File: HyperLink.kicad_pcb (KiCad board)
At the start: 2 copper layers, 35 x 24 mm, 41 parts, among them J1 USB_C_Receptacle_USB2.0, J2 Conn_02x05_Odd_Even, J3 Conn_02x05_Odd_Even, SW1 SW_Push, U1 ESP32-C3, U2 LM2937xMP, Y1 ABM11W-40.0000MHZ-8-B1U-T3

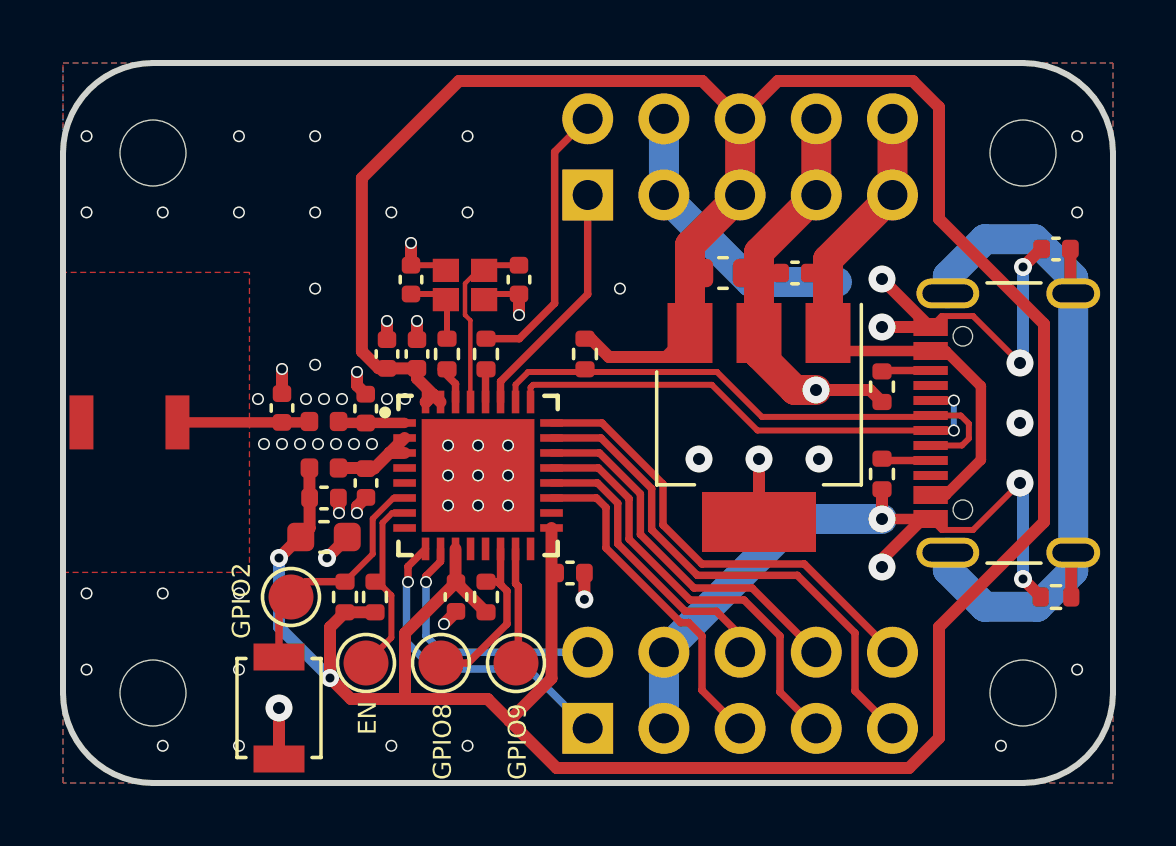
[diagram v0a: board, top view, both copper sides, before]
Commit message: Replace LDO and add USB TVS diode
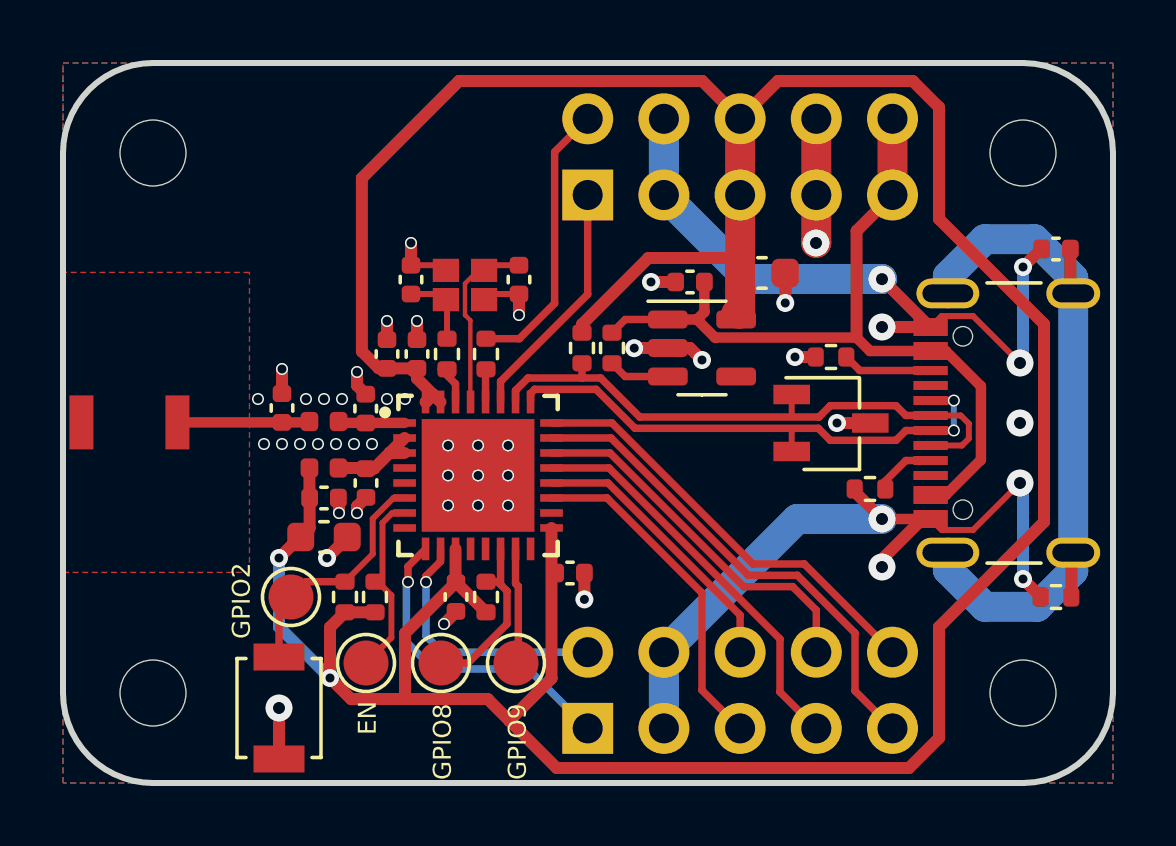
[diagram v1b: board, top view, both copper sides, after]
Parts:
- removed C13: 10u, Capacitor_SMD:C_0603_1608Metric
- added C7: 10u, Capacitor_SMD:C_0603_1608Metric, F.Cu at (142.3, 77.0)
- added R10: 10k, Resistor_SMD:R_0402_1005Metric, F.Cu at (137.3, 79.5)
- added U3: MIC5504-3.3YM5, Package_TO_SOT_SMD:SOT-23-5, F.Cu at (140.3, 79.5)
- C12: value 100n -> 1u
- U2: value LM2937xMP -> PESD2USB5UXT; footprint Package_TO_SOT_SMD:SOT-223-3_TabPin2 -> Package_TO_SOT_SMD:TSOT-23
- moved C12 3.51 mm to (139.9, 77.3)
- moved U2 2.40 mm to (144.6, 82.0), turned to 0 degrees
- moved R7 1.97 mm to (144.6, 79.8), turned to 180 degrees
- moved R8 0.64 mm to (145.9, 84.2), turned to 180 degrees
- moved R9 0.22 mm to (136.3, 79.5)
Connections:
- U2 pad 1: VBUS -> /USB_D+
- U2 pad 2: GND -> /USB_D-
- U2 pad 3: +3V3 -> GND
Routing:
- net VBUS: track 18.5 -> 27.2 mm
- net GND: track 74.6 -> 70.0 mm, vias 73 -> 50
- net /LDO_EN: track 0.00 -> 2.04 mm
- net /CC2: track 1.63 -> 3.00 mm
- net /USB_D+: track 18.5 -> 19.8 mm
- net +3V3: track 115.1 -> 116.2 mm
- net /GPIO14: track 14.3 -> 13.5 mm
- net /GPIO17: track 15.3 -> 14.5 mm
- net /GPIO16: track 17.3 -> 16.5 mm
- net /USB_D-: track 17.0 -> 17.8 mm

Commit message: Add status LEDs
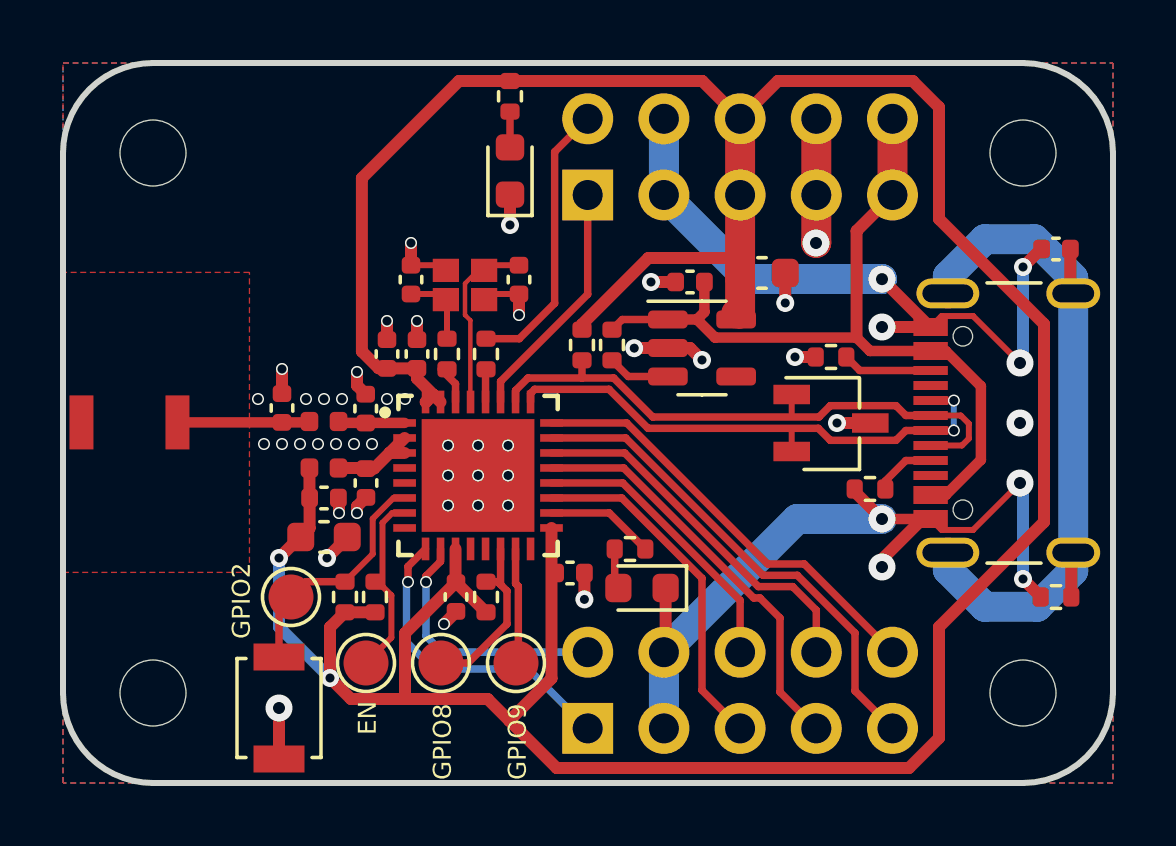
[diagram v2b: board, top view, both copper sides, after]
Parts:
- added D1: LED, LED_SMD:LED_0603_1608Metric, F.Cu at (138.3, 87.5)
- added D2: LED, LED_SMD:LED_0603_1608Metric, F.Cu at (133.9, 73.6)
- added R11: 1k, Resistor_SMD:R_0402_1005Metric, F.Cu at (137.9, 86.2)
- added R12: 1k, Resistor_SMD:R_0402_1005Metric, F.Cu at (133.9, 71.1)
- moved R10 0.10 mm to (137.3, 79.4)
- moved R9 0.10 mm to (136.3, 79.4)
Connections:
- U1 pad 18: unconnected-(U1-VDD_SPI-Pad18) -> /STATUS_LED
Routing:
- net /STATUS_LED: track 0.00 -> 3.62 mm
- net GND: track 70.0 -> 73.2 mm, vias 50 -> 51
- net /STATUS_LED_RES: track 0.00 -> 1.35 mm
- net /POWER_LED_RES: track 0.00 -> 1.19 mm

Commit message: Tie SHIELD directly to GND
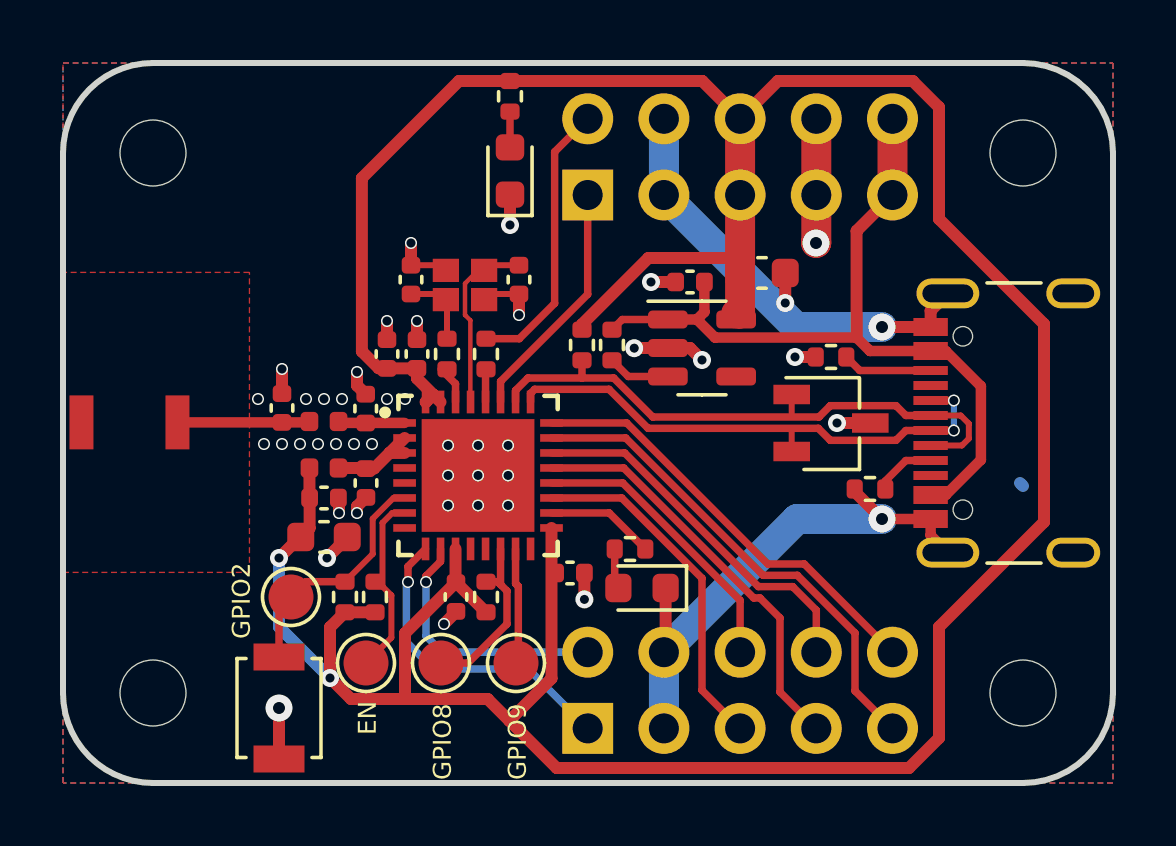
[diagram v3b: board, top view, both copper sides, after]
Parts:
- removed C11: C, Capacitor_SMD:C_0402_1005Metric
- removed R1: R, Resistor_SMD:R_0402_1005Metric
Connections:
- J1 pad S1: /SHIELD -> GND
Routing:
- net /SHIELD: track 24.4 -> 0.00 mm
- net GND: track 73.2 -> 56.2 mm, vias 51 -> 44

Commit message: Fix last remaining TODOs and clean up schematic
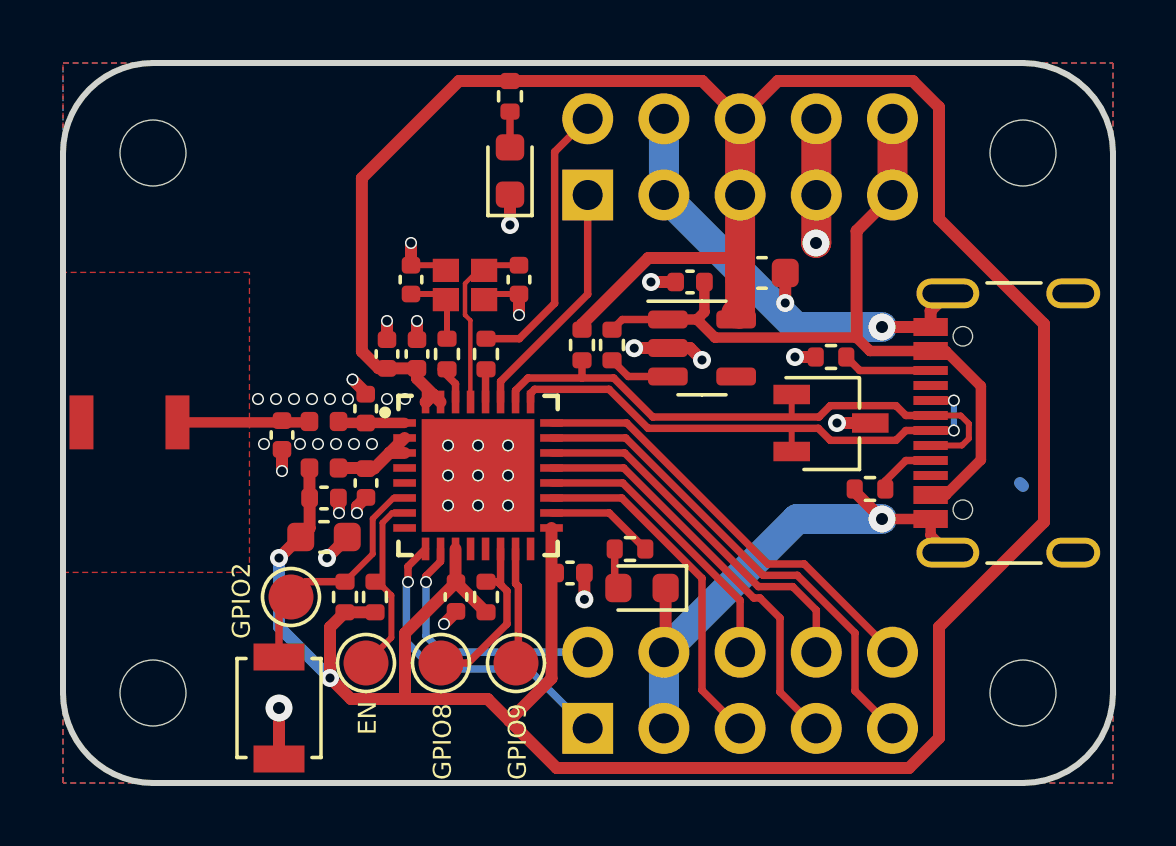
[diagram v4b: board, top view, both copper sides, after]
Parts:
- moved C14 0.90 mm to (126.3, 82.4), turned to -90 degrees
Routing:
- net GND: track 56.2 -> 55.9 mm, vias 44 -> 45
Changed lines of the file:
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@@
   )
   (footprint "Capacitor_SMD:C_0402_1005Metric" (layer "F.Cu")
-    (at 126.3 81.5 90)
+    (at 126.3 82.4 -90)
     (descr "Capacitor SMD 0402 (1005 Metric), square (rectangular) end terminal, IPC_7351 nominal, (Body size source: IPC-SM-782 page 76, https://www.pcb-3d.com/wordpress/wp-content/uploads/ipc-sm-782a_amendment_1_and_2.pdf), generated with kicad-footprint-generator")
     (tags "capacitor")
@@
     (fp_line (start 0.5 0.25) (end -0.5 0.25)
       (stroke (width 0.1) (type solid)) (layer "F.Fab"))
-    (pad "1" smd roundrect (at -0.48 0 90) (size 0.56 0.62) (layers "F.Cu" "F.Paste" "F.Mask") (roundrect_rratio 0.25)
+    (pad "1" smd roundrect (at -0.48 0 270) (size 0.56 0.62) (layers "F.Cu" "F.Paste" "F.Mask") (roundrect_rratio 0.25)
       (net 17 "/RF") (pintype "passive"))
-    (pad "2" smd roundrect (at 0.48 0 90) (size 0.56 0.62) (layers "F.Cu" "F.Paste" "F.Mask") (roundrect_rratio 0.25)
+    (pad "2" smd roundrect (at 0.48 0 270) (size 0.56 0.62) (layers "F.Cu" "F.Paste" "F.Mask") (roundrect_rratio 0.25)
       (net 5 "GND") (pintype "passive"))
     (model "${KICAD6_3DMODEL_DIR}/Capacitor_SMD.3dshapes/C_0402_1005Metric.wrl"
@@
   (segment (start 147.92 85.745) (end 148.495 86.32) (width 0.35) (layer "F.Cu") (net 5))
   (segment (start 147.92 85.2) (end 147.92 85.745) (width 0.35) (layer "F.Cu") (net 5))
+  (segment (start 128.65 80.55) (end 129.09 80.99) (width 0.4) (layer "F.Cu") (net 5))
   (segment (start 133.9 74.3875) (end 133.9 75.4) (width 0.4) (layer "F.Cu") (net 5))
   (segment (start 139.42 77.3) (end 138.6 77.3) (width 0.4) (layer "F.Cu") (net 5))
   (segment (start 130.8 79.22) (end 130.8 78.6) (width 0.4) (layer "F.Cu") (net 5))
+  (segment (start 129.09 80.99) (end 129.09 81.04) (width 0.4) (layer "F.Cu") (net 5))
   (segment (start 131.7 88.7) (end 132.1 88.3) (width 0.4) (layer "F.Cu") (net 5))
   (segment (start 128.2 84.52) (end 128.18 84.5) (width 0.4) (layer "F.Cu") (net 5))
@@
   (segment (start 145.91 82) (end 144.8 82) (width 0.4) (layer "F.Cu") (net 5))
   (segment (start 130.6 76.74) (end 131.590001 76.74) (width 0.2) (layer "F.Cu") (net 5))
-  (segment (start 128.8 80.75) (end 129.09 81.04) (width 0.4) (layer "F.Cu") (net 5))
   (segment (start 143.075 78) (end 143.075 77) (width 0.4) (layer "F.Cu") (net 5))
   (segment (start 145.39 84.29) (end 146.3 85.2) (width 0.4) (layer "F.Cu") (net 5))
@@
   (segment (start 134.2 78.4) (end 134.2 77.7) (width 0.4) (layer "F.Cu") (net 5))
   (segment (start 140.3 79.9) (end 139.9 79.5) (width 0.4) (layer "F.Cu") (net 5))
-  (segment (start 126.3 80.2) (end 126.3 81.02) (width 0.4) (layer "F.Cu") (net 5))
   (segment (start 136.38 87.88) (end 136.38 87) (width 0.4) (layer "F.Cu") (net 5))
   (segment (start 130.6 76) (end 130.6 76.7) (width 0.4) (layer "F.Cu") (net 5))
+  (segment (start 126.3 82.88) (end 126.3 83.6) (width 0.4) (layer "F.Cu") (net 5))
   (segment (start 127.8 86.5) (end 128.475 85.825) (width 0.4) (layer "F.Cu") (net 5))
   (segment (start 147.92 78.255) (end 148.495 77.68) (width 0.4) (layer "F.Cu") (net 5))
   (segment (start 134.2 77.7) (end 133.224001 77.7) (width 0.2) (layer "F.Cu") (net 5))
   (segment (start 138.040639 79.505918) (end 138.046557 79.5) (width 0.4) (layer "F.Cu") (net 5))
-  (segment (start 128.8 80.3) (end 128.8 80.75) (width 0.4) (layer "F.Cu") (net 5))
   (segment (start 144.11 74.4) (end 144.11 75.99) (width 1) (layer "F.Cu") (net 5))
   (segment (start 128.799503 85) (end 128.799503 84.780497) (width 0.4) (layer "F.Cu") (net 5))
@@
   (segment (start 144.11 75.99) (end 144.1 76) (width 1) (layer "F.Cu") (net 5))
   (via (at 130.4 81.2) (size 0.4) (drill 0.3) (layers "F.Cu" "B.Cu") (free) (net 5))
-  (via (at 128.8 80.3) (size 0.4) (drill 0.3) (layers "F.Cu" "B.Cu") (free) (net 5))
+  (via (at 128.65 80.55) (size 0.4) (drill 0.3) (layers "F.Cu" "B.Cu") (free) (net 5))
   (via (at 126.9 82.7) (size 0.4) (drill 0.3) (layers "F.Cu" "B.Cu") (free) (net 5))
   (via (at 138.6 77.3) (size 0.6) (drill 0.3) (layers "F.Cu" "B.Cu") (net 5))
@@
   (via (at 146.3 78.8) (size 0.9) (drill 0.4) (layers "F.Cu" "B.Cu") (free) (net 5))
   (via (at 133.834851 84.7487) (size 0.4) (drill 0.3) (layers "F.Cu" "B.Cu") (net 5))
+  (via (at 126.7 81.2) (size 0.4) (drill 0.3) (layers "F.Cu" "B.Cu") (free) (net 5))
   (via (at 134.2 78.4) (size 0.4) (drill 0.3) (layers "F.Cu" "B.Cu") (free) (net 5))
   (via (at 132.834851 83.7487) (size 0.4) (drill 0.3) (layers "F.Cu" "B.Cu") (net 5))
@@
   (via (at 133.834851 83.7487) (size 0.4) (drill 0.3) (layers "F.Cu" "B.Cu") (net 5))
   (via (at 131.834851 82.7487) (size 0.4) (drill 0.3) (layers "F.Cu" "B.Cu") (net 5))
-  (via (at 127.1 81.2) (size 0.4) (drill 0.3) (layers "F.Cu" "B.Cu") (free) (net 5))
+  (via (at 127.3 81.2) (size 0.4) (drill 0.3) (layers "F.Cu" "B.Cu") (free) (net 5))
   (via (at 128.7 82.7) (size 0.4) (drill 0.3) (layers "F.Cu" "B.Cu") (free) (net 5))
   (via (at 129.8 78.6) (size 0.4) (drill 0.3) (layers "F.Cu" "B.Cu") (free) (net 5))
   (via (at 132.834851 84.7487) (size 0.4) (drill 0.3) (layers "F.Cu" "B.Cu") (net 5))
+  (via (at 126.3 83.6) (size 0.4) (drill 0.3) (layers "F.Cu" "B.Cu") (free) (net 5))
   (via (at 130.8 78.6) (size 0.4) (drill 0.3) (layers "F.Cu" "B.Cu") (free) (net 5))
   (via (at 146.3 85.2) (size 0.9) (drill 0.4) (layers "F.Cu" "B.Cu") (free) (net 5))
@@
   (via (at 128.2 85) (size 0.4) (drill 0.3) (layers "F.Cu" "B.Cu") (free) (net 5))
   (via (at 129.3 82.7) (size 0.4) (drill 0.3) (layers "F.Cu" "B.Cu") (free) (net 5))
-  (via (at 126.3 80.2) (size 0.4) (drill 0.3) (layers "F.Cu" "B.Cu") (free) (net 5))
+  (via (at 126.099503 81.2) (size 0.4) (drill 0.3) (layers "F.Cu" "B.Cu") (free) (net 5))
   (via (at 144.1 76) (size 0.9) (drill 0.4) (layers "F.Cu" "B.Cu") (free) (net 5))
   (via (at 133.834851 82.7487) (size 0.4) (drill 0.3) (layers "F.Cu" "B.Cu") (net 5))
-  (via (at 126.3 82.7) (size 0.4) (drill 0.3) (layers "F.Cu" "B.Cu") (free) (net 5))
   (via (at 125.5 81.2) (size 0.4) (drill 0.3) (layers "F.Cu" "B.Cu") (free) (net 5))
   (via (at 131.7 88.7) (size 0.4) (drill 0.3) (layers "F.Cu" "B.Cu") (free) (net 5))
-  (via (at 127.7 81.2) (size 0.4) (drill 0.3) (layers "F.Cu" "B.Cu") (free) (net 5))
-  (via (at 128.3 81.2) (size 0.4) (drill 0.3) (layers "F.Cu" "B.Cu") (free) (net 5))
+  (via (at 127.9 81.2) (size 0.4) (drill 0.3) (layers "F.Cu" "B.Cu") (free) (net 5))
+  (via (at 128.5 81.2) (size 0.4) (drill 0.3) (layers "F.Cu" "B.Cu") (free) (net 5))
   (via (at 127.8 86.5) (size 0.6) (drill 0.3) (layers "F.Cu" "B.Cu") (free) (net 5))
   (segment (start 143.43 78.8) (end 146.3 78.8) (width 1) (layer "B.Cu") (net 5))

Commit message: Replace Antenna symbol with chip antenna
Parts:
- C1: value C -> 4.7p
- C14: value C -> 4p
- C5, C6: value 12pF -> 10pF
- L1: value L -> 1.8nH
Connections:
- AE1 pad 2: (no net) -> unconnected-(AE1-PCB_Trace-Pad2)
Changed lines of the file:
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@@
   (net 40 "/POWER_LED_RES")
   (net 41 "/STATUS_LED")
+  (net 42 "unconnected-(AE1-PCB_Trace-Pad2)")
   (footprint "Package_TO_SOT_SMD:SOT-23-5" (layer "F.Cu")
     (at 140.3 79.5)
@@
         (effects (font (size 1 1) (thickness 0.15)))
     )
-    (fp_text value "12pF" (at 0 1.16 90) (layer "F.Fab") hide
+    (fp_text value "10pF" (at 0 1.16 90) (layer "F.Fab") hide
         (effects (font (size 1 1) (thickness 0.15)))
     )
@@
         (effects (font (size 1 1) (thickness 0.15)))
     )
-    (fp_text value "C" (at 0 1.16 90) (layer "F.Fab") hide
+    (fp_text value "4p" (at 0 1.16 90) (layer "F.Fab") hide
         (effects (font (size 1 1) (thickness 0.15)))
     )
@@
         (effects (font (size 1 1) (thickness 0.15)))
     )
-    (fp_text value "C" (at 0 1.16 90) (layer "F.Fab") hide
+    (fp_text value "4.7p" (at 0 1.16 90) (layer "F.Fab") hide
         (effects (font (size 1 1) (thickness 0.15)))
     )
@@
         (effects (font (size 1 1) (thickness 0.15)))
     )
-    (fp_text value "L" (at 0 1.17) (layer "F.Fab") hide
+    (fp_text value "1.8nH" (at 0 1.17) (layer "F.Fab") hide
         (effects (font (size 1 1) (thickness 0.15)))
     )
@@
         (effects (font (size 1 1) (thickness 0.15)))
     )
-    (fp_text value "12pF" (at 0 1.16 90) (layer "F.Fab") hide
+    (fp_text value "10pF" (at 0 1.16 90) (layer "F.Fab") hide
         (effects (font (size 1 1) (thickness 0.15)))
     )
@@
     (property "Sheetfile" "HyperLink.kicad_sch")
     (property "Sheetname" "")
-    (property "ki_description" "Antenna")
+    (property "ki_description" "Ceramic chip antenna with pin for PCB trace")
     (property "ki_keywords" "antenna")
     (attr smd)
@@
       (stroke (width 0.1) (type default)) (layer "F.CrtYd"))
     (pad "1" smd rect locked (at 4.1 0) (size 0.8 1.8) (layers "F.Cu" "F.Paste" "F.Mask")
-      (net 17 "/RF") (pinfunction "A") (pintype "input") (thermal_bridge_angle 45))
+      (net 17 "/RF") (pinfunction "FEED") (pintype "input") (thermal_bridge_angle 45))
     (pad "2" smd rect locked (at 0.9 0) (size 0.8 1.8) (layers "F.Cu" "F.Paste" "F.Mask")
-      (thermal_bridge_angle 45))
+      (net 42 "unconnected-(AE1-PCB_Trace-Pad2)") (pinfunction "PCB_Trace") (pintype "passive+no_connect") (thermal_bridge_angle 45))
     (zone (net 0) (net_name "") (layers "*.Cu") (hatch edge 0.5)
       (connect_pads (clearance 0))
